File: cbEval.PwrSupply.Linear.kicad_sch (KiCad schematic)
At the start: 38 parts, among them J1 CAL.CT3151V1-0, J10 Socket.Hor.2x5.6-5535512-4, J2 CAL.CT3151V1-2, J3 Keystone.4918, J4 Keystone.4918, J5 Keystone.3571, J6 Keystone.3571, J7 Socket.Hor.2x5.6-5535512-4, J8 Header.Hor.2x5.9-103326-0-05, J9 Header.Hor.2x5.9-103326-0-05, U1 MIC29151-5.0WU, U2 MIC29151-3.3WU, U3 DS1834AS+

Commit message: Bus-Leitungen neu belegt
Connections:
- net PwrBus-Rsrvd0 is gone; now on net I2C-SDA: J7.9, J8.9
- net PwrBus-Rsrvd1 is gone; now on net I2C-SCL: J7.10, J8.10
- net I2C-SCL: no longer J10.10, J9.10
- net I2C-SDA: no longer J10.9, J9.9
- new net One-Wire: J10.10, J9.10
- new net SPI-ADR2: J10.9, J9.9
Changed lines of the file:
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@@
     (stroke (width 0) (type solid) (color 0 0 0 0))
   )
-  (label "PwrBus-Rsrvd0" (at 53.34 182.88 0)
+  (label "I2C-SDA" (at 45.72 182.88 0)
     (effects (font (size 1.27 1.27)) (justify left bottom))
   )
-  (label "PwrBus-Rsrvd1" (at 53.34 185.42 0)
+  (label "I2C-SCL" (at 45.72 185.42 0)
     (effects (font (size 1.27 1.27)) (justify left bottom))
   )
@@
     (effects (font (size 1.27 1.27)) (justify left bottom))
   )
-  (label "I2C-SDA" (at 119.38 182.88 0)
+  (label "SPI-ADR2" (at 119.38 182.88 0)
     (effects (font (size 1.27 1.27)) (justify left bottom))
   )
-  (label "I2C-SCL" (at 119.38 185.42 0)
+  (label "One-Wire" (at 119.38 185.42 0)
     (effects (font (size 1.27 1.27)) (justify left bottom))
   )
@@
     (pin "1")
   )
-  (symbol (lib_name "Supply:GND_6") (lib_id "Supply:GND") (at 35.56 101.6 0) (unit 1)
+  (symbol (lib_id "Supply:GND") (at 35.56 101.6 0) (unit 1)
     (in_bom yes) (on_board yes)
     (property "Reference" "#PWR01" (id 0) (at 35.56 106.68 0)
@@
     (pin "1")
   )
-  (symbol (lib_name "Supply:GND_10") (lib_id "Supply:GND") (at 71.12 101.6 0) (unit 1)
+  (symbol (lib_id "Supply:GND") (at 71.12 101.6 0) (unit 1)
     (in_bom yes) (on_board yes)
     (property "Reference" "#PWR04" (id 0) (at 71.12 106.68 0)
@@
     (pin "1")
   )
-  (symbol (lib_name "Supply:GND_9") (lib_id "Supply:GND") (at 104.14 55.88 0) (unit 1)
+  (symbol (lib_id "Supply:GND") (at 104.14 55.88 0) (unit 1)
     (in_bom yes) (on_board yes)
     (property "Reference" "#PWR07" (id 0) (at 104.14 60.96 0)
@@
     (pin "1")
   )
-  (symbol (lib_name "Supply:GND_4") (lib_id "Supply:GND") (at 127 55.88 0) (unit 1)
+  (symbol (lib_id "Supply:GND") (at 127 55.88 0) (unit 1)
     (in_bom yes) (on_board yes)
     (property "Reference" "#PWR09" (id 0) (at 127 60.96 0)
@@
     (pin "1")
   )
-  (symbol (lib_name "Supply:GND_1") (lib_id "Supply:GND") (at 127 101.6 0) (unit 1)
+  (symbol (lib_id "Supply:GND") (at 127 101.6 0) (unit 1)
     (in_bom yes) (on_board yes)
     (property "Reference" "#PWR011" (id 0) (at 127 106.68 0)
@@
     (pin "1")
   )
-  (symbol (lib_name "Supply:GND_3") (lib_id "Supply:GND") (at 165.1 55.88 0) (unit 1)
+  (symbol (lib_id "Supply:GND") (at 165.1 55.88 0) (unit 1)
     (in_bom yes) (on_board yes)
     (property "Reference" "#PWR013" (id 0) (at 165.1 60.96 0)
@@
     (pin "1")
   )
-  (symbol (lib_name "Supply:GND_2") (lib_id "Supply:GND") (at 165.1 101.6 0) (unit 1)
+  (symbol (lib_id "Supply:GND") (at 165.1 101.6 0) (unit 1)
     (in_bom yes) (on_board yes)
     (property "Reference" "#PWR014" (id 0) (at 165.1 106.68 0)
@@
     (pin "1")
   )
-  (symbol (lib_name "Supply:GND_7") (lib_id "Supply:GND") (at 193.04 55.88 0) (unit 1)
+  (symbol (lib_id "Supply:GND") (at 193.04 55.88 0) (unit 1)
     (in_bom yes) (on_board yes)
     (property "Reference" "#PWR015" (id 0) (at 193.04 60.96 0)
@@
     (pin "1")
   )
-  (symbol (lib_name "Supply:GND_8") (lib_id "Supply:GND") (at 193.04 101.6 0) (unit 1)
+  (symbol (lib_id "Supply:GND") (at 193.04 101.6 0) (unit 1)
     (in_bom yes) (on_board yes)
     (property "Reference" "#PWR016" (id 0) (at 193.04 106.68 0)
@@
       (effects (font (size 0.635 0.635) italic))
     )
-    (property "Usage" "GND Extension" (id 5) (at 25.4 86.36 0))
-    (pin "1")
-  )
-  (symbol (lib_name "J.QuickConnect:Keystone.4918_1") (lib_id "J.QuickConnect:Keystone.4918") (at 27.94 96.52 0) (mirror y) (unit 1)
+    (property "Usage" "GND Extension" (id 6) (at 25.4 86.36 0))
+    (pin "1")
+  )
+  (symbol (lib_id "J.QuickConnect:Keystone.4918") (at 27.94 96.52 0) (mirror y) (unit 1)
     (in_bom yes) (on_board yes)
     (property "Reference" "J4" (id 0) (at 25.4 91.44 0))
@@
       (effects (font (size 0.635 0.635) italic))
     )
-    (property "Usage" "GND Extension" (id 5) (at 25.4 99.06 0))
+    (property "Usage" "GND Extension" (id 6) (at 25.4 99.06 0))
     (pin "1")
   )
@@
       (effects (font (size 0.635 0.635) italic))
     )
-    (property "Usage" "GND Extension" (id 5) (at 45.72 86.36 0))
-    (pin "1")
-  )
-  (symbol (lib_name "J.QuickConnect:Keystone.3571_1") (lib_id "J.QuickConnect:Keystone.3571") (at 43.18 96.52 0) (unit 1)
+    (property "Usage" "GND Extension" (id 6) (at 45.72 86.36 0))
+    (pin "1")
+  )
+  (symbol (lib_id "J.QuickConnect:Keystone.3571") (at 43.18 96.52 0) (unit 1)
     (in_bom yes) (on_board yes)
     (property "Reference" "J6" (id 0) (at 45.72 91.44 0))
@@
       (effects (font (size 0.635 0.635) italic))
     )
-    (property "Usage" "GND Extension" (id 5) (at 45.72 99.06 0))
+    (property "Usage" "GND Extension" (id 6) (at 45.72 99.06 0))
     (pin "1")
   )
@@
       (effects (font (size 0.635 0.635) italic))
     )
-    (property "Usage" "Pwr Supply V+" (id 6) (at 71.12 35.56 0))
-    (pin "1")
-  )
+    (property "Usage" "Pwr Supply V+" (id 7) (at 71.12 35.56 0))
+    (pin "1")
+  )

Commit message: Bauteil (PinHeader) ausgetauscht
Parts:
- J11: renamed from JP3; symbol JP:Bergstik-II_6 -> J.PinHeader:Bergstik-II_6
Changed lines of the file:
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@@
     (pin "6")
   )
-  (symbol (lib_id "JP:Bergstik-II_6") (at 43.18 40.64 0) (unit 1)
-    (in_bom yes) (on_board yes)
-    (property "Reference" "JP3" (id 0) (at 40.64 50.8 0)
+  (symbol (lib_id "J.PinHeader:Bergstik-II_6") (at 43.18 40.64 0) (unit 1)
+    (in_bom yes) (on_board yes)
+    (property "Reference" "J11" (id 0) (at 40.64 50.8 0)
       (effects (font (size 1.27 1.27)) (justify left))
     )
@@
     )
     (path "/fae6516a-9429-461a-8ec1-3b1a99f8be92"
-      (reference "JP3") (unit 1) (value "Bergstik-II_6") (footprint "Connector_PinHeader_2.54mm:PinHeader_1x06_P2.54mm_Vertical")
+      (reference "J11") (unit 1) (value "Bergstik-II_6") (footprint "Connector_PinHeader_2.54mm:PinHeader_1x06_P2.54mm_Vertical")
     )
     (path "/aa3513d0-0eee-457c-a792-7c9954431f2c"

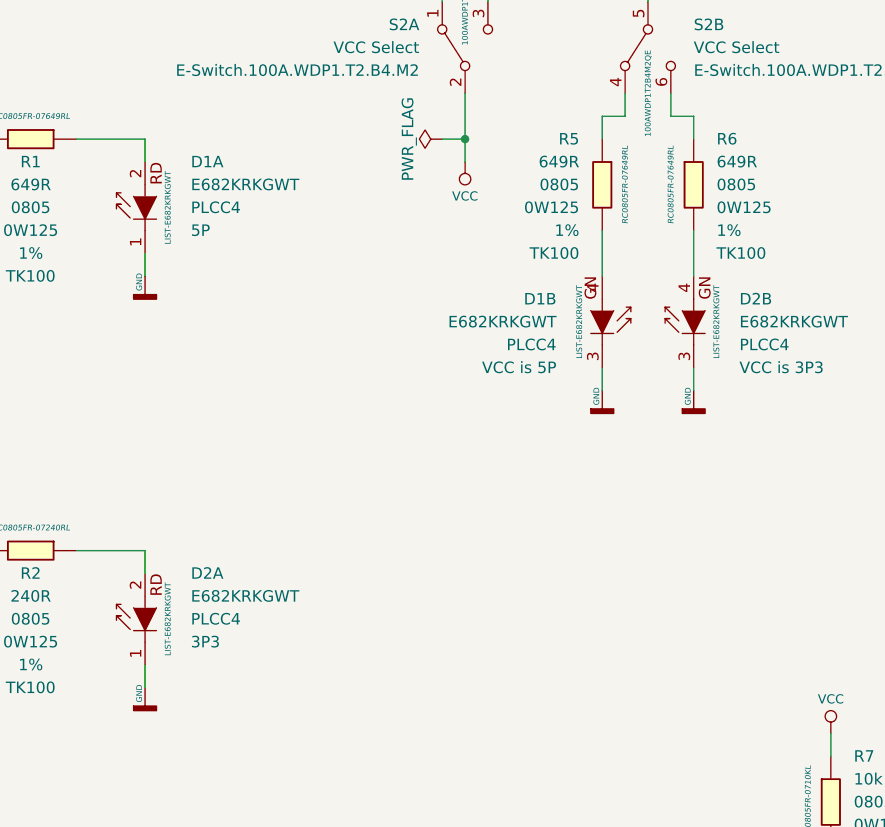
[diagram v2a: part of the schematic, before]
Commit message: kleinere Korrekturen vor Bauteilbestellung
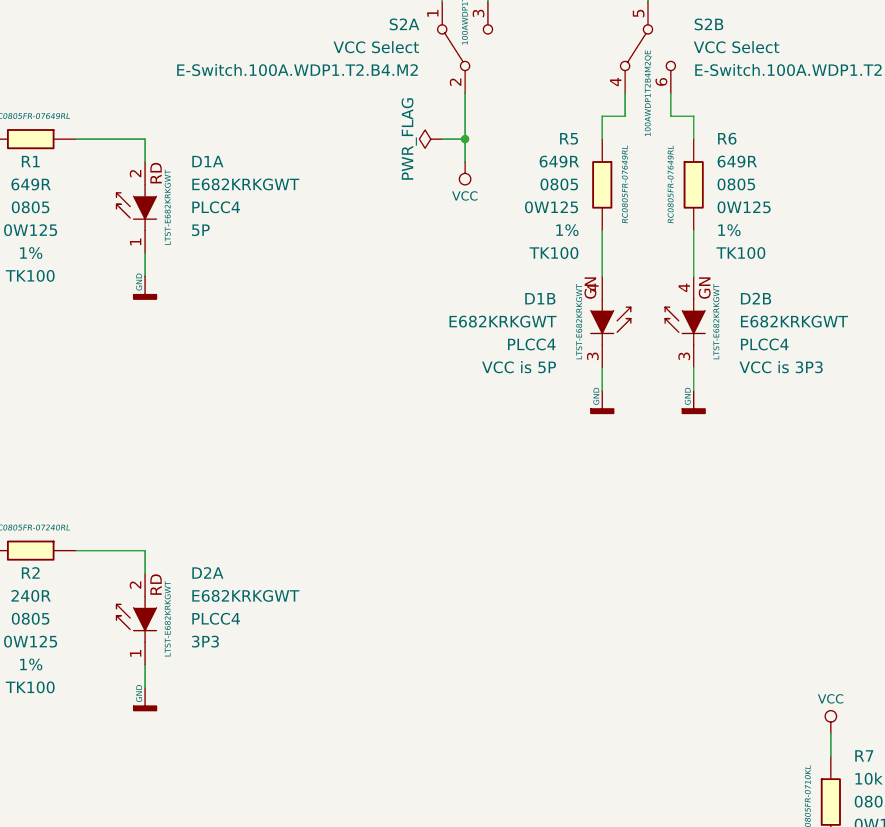
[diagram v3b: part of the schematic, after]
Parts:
- D1, D2: ID LIST-E682KRKGWT -> LTST-E682KRKGWT
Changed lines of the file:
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@@
     (pin "1")
   )
-  (symbol (lib_id "D.LED:E682KRKGWT") (at 193.04 48.26 0) (unit 1)
+  (symbol (lib_name "D.LED:E682KRKGWT_1") (lib_id "D.LED:E682KRKGWT") (at 193.04 48.26 0) (unit 1)
     (in_bom yes) (on_board yes)
     (property "Reference" "D1" (id 0) (at 198.12 43.18 0)
@@
       (effects (font (size 1.27 1.27)) (justify left))
     )
-    (property "ID" "LIST-E682KRKGWT" (id 5) (at 195.58 48.26 90)
+    (property "ID" "LTST-E682KRKGWT" (id 5) (at 195.58 48.26 90)
       (effects (font (size 0.635 0.635)))
     )
@@
       (effects (font (size 1.27 1.27)) (justify left))
     )
-    (property "ID" "LIST-E682KRKGWT" (id 5) (at 195.58 93.98 90)
+    (property "ID" "LTST-E682KRKGWT" (id 5) (at 195.58 93.98 90)
       (effects (font (size 0.635 0.635)))
     )
@@
     (pin "2")
   )
-  (symbol (lib_id "D.LED:E682KRKGWT") (at 243.84 60.96 0) (mirror y) (unit 2)
+  (symbol (lib_name "D.LED:E682KRKGWT_2") (lib_id "D.LED:E682KRKGWT") (at 243.84 60.96 0) (mirror y) (unit 2)
     (in_bom yes) (on_board yes)
     (property "Reference" "D1" (id 0) (at 238.76 58.42 0)
@@
       (effects (font (size 1.27 1.27)) (justify left))
     )
-    (property "ID" "LIST-E682KRKGWT" (id 5) (at 241.3 60.96 90)
+    (property "ID" "LTST-E682KRKGWT" (id 5) (at 241.3 60.96 90)
       (effects (font (size 0.635 0.635)))
     )
@@
     (pin "4")
   )
-  (symbol (lib_id "D.LED:E682KRKGWT") (at 254 60.96 0) (unit 2)
+  (symbol (lib_name "D.LED:E682KRKGWT_3") (lib_id "D.LED:E682KRKGWT") (at 254 60.96 0) (unit 2)
     (in_bom yes) (on_board yes)
     (property "Reference" "D2" (id 0) (at 259.08 58.42 0)
@@
       (effects (font (size 1.27 1.27)) (justify left))
     )
-    (property "ID" "LIST-E682KRKGWT" (id 5) (at 256.54 60.96 90)
+    (property "ID" "LTST-E682KRKGWT" (id 5) (at 256.54 60.96 90)
       (effects (font (size 0.635 0.635)))
     )

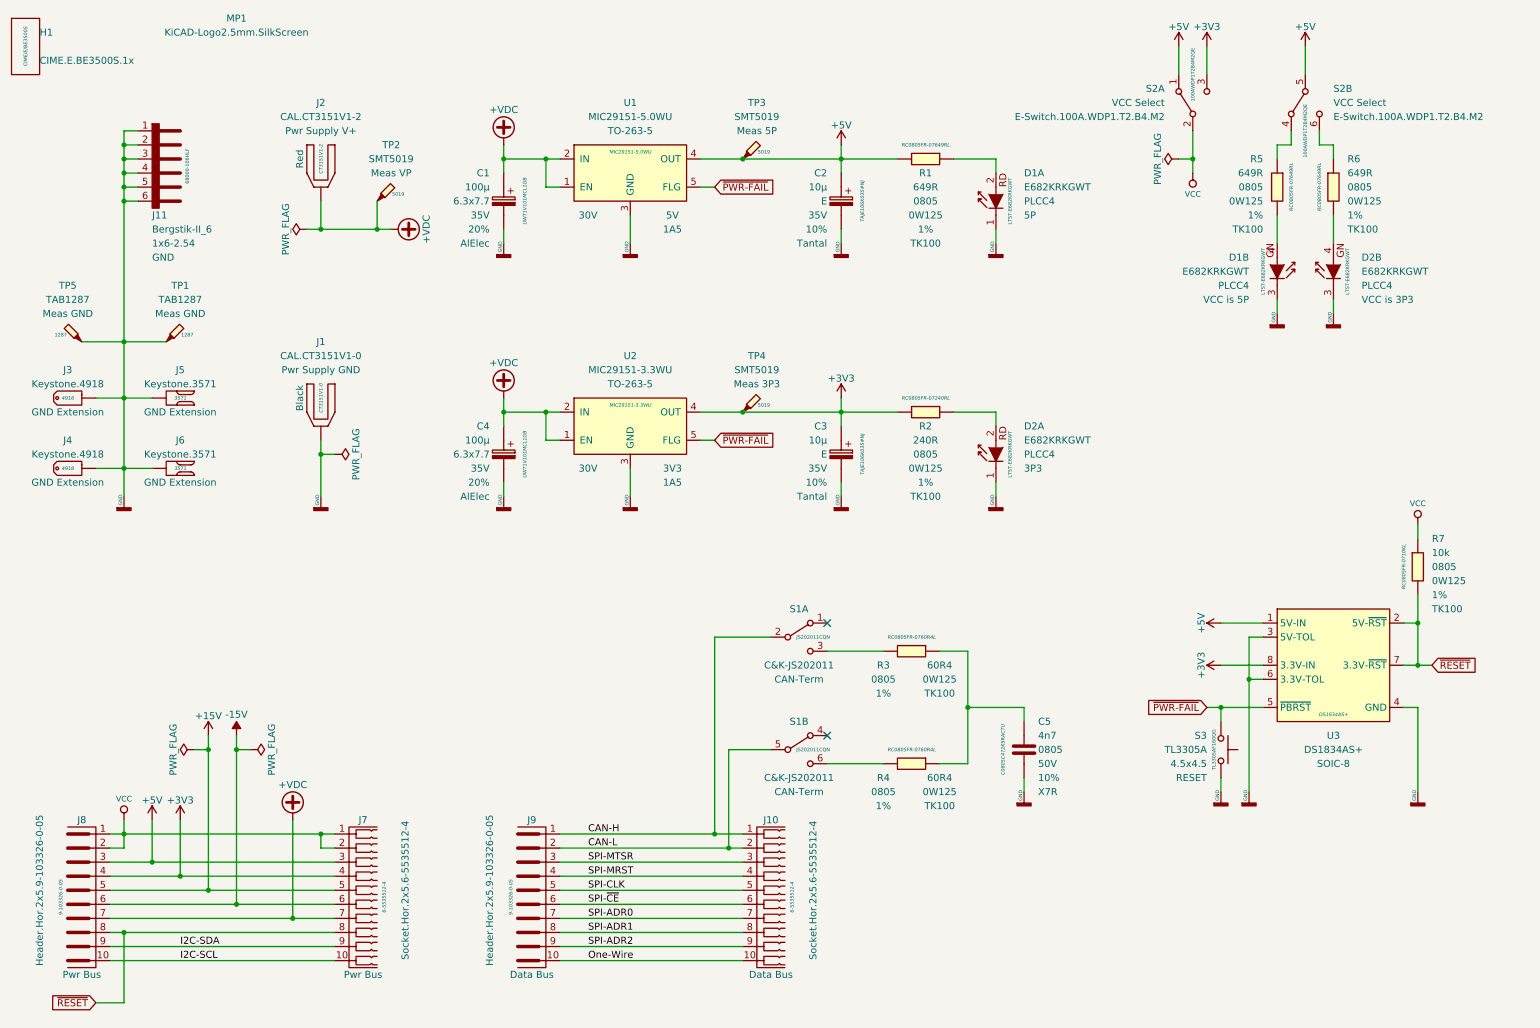
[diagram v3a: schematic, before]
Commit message: Bus-Stecker getauscht
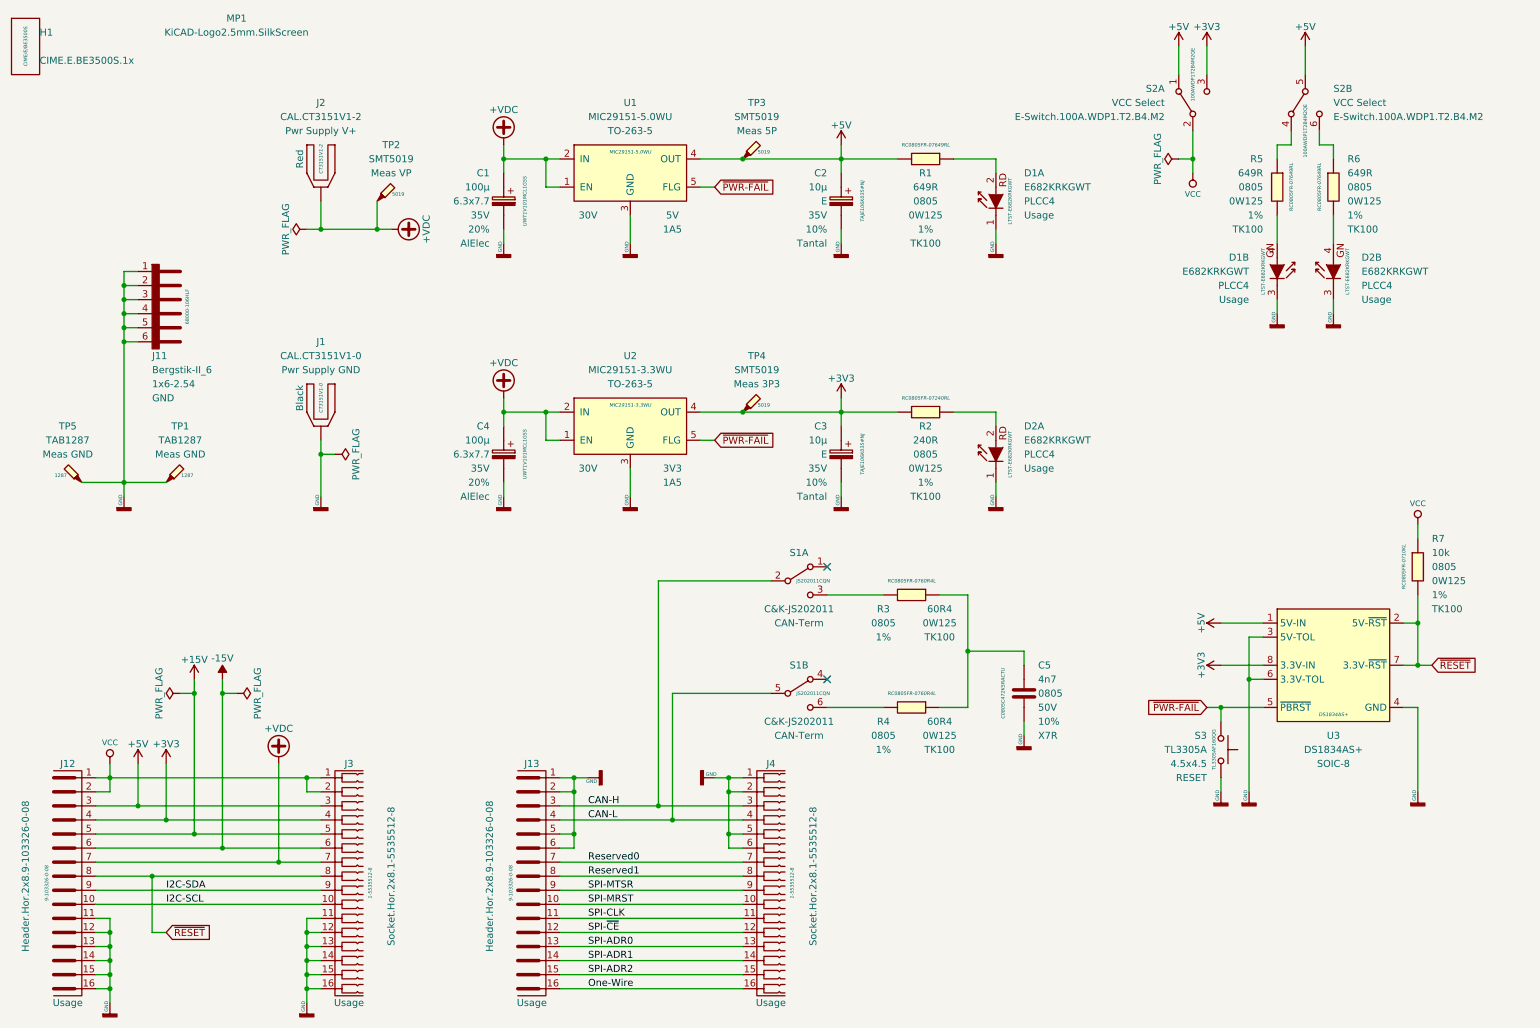
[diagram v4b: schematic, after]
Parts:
- removed J10, J7: Socket.Hor.2x5.6-5535512-4, BTech.Connector.AMPMODU-ModII:Socket.Hor.2x5.6-5535512-4, symbol J.AMPMODU-ModII:Socket.Hor.2x5.6-5535512-4
- removed J3, J4: Keystone.4918, BTech.Connector.QuickConnect:Keystone.4918, symbol J.QuickConnect:Keystone.4918
- removed J5, J6: Keystone.3571, BTech.Connector.QuickConnect:Keystone.3571, symbol J.QuickConnect:Keystone.3571
- removed J8, J9: Header.Hor.2x5.9-103326-0-05, Connector_PinHeader_2.54mm:PinHeader_2x05_P2.54mm_Horizontal, symbol J.AMPMODU-ModII:Header.Hor.2x5.9-103326-0-05
- added J12, J13: Header.Hor.2x8.9-103326-0-08, Connector_PinHeader_2.54mm:PinHeader_2x08_P2.54mm_Horizontal, symbol J.AMPMODU-ModII:Header.Hor.2x8.9-103326-0-08
- added J3, J4: Socket.Hor.2x8.1-5535512-8, BTech.Connector.AMPMODU-ModII:Socket.Hor.2x5.6-5535512-4, symbol J.AMPMODU-ModII:Socket.Hor.2x8.1-5535512-8
- C1, C4: ID UWT1V101MCL1GB -> UWT1V101MCL1G5S
- D1: Usage VCC is 5P -> Usage
- D1: Usage 5P -> Usage
- D2: Usage 3P3 -> Usage
- D2: Usage VCC is 3P3 -> Usage
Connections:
- net +15V: now also J12.5, J3.5
- net +3V3: now also J12.4, J3.4
- net +5V: now also J12.3, J3.3
- net +VDC: now also J12.7, J3.7
- net -15V: now also J12.6, J3.6
- net CAN-H: now also J13.3, J4.3
- net CAN-L: now also J13.4, J4.4
- net GND: now also J12.11, J12.12, J12.13, J12.14, J12.15, J12.16, J13.1, J13.2, J13.5, J13.6, J3.11, J3.12, J3.13, J3.14, J3.15, J3.16, J4.1, J4.2, J4.5, J4.6
- net I2C-SCL: now also J12.10, J3.10
- net I2C-SDA: now also J12.9, J3.9
- net One-Wire: now also J13.16, J4.16
- net SPI-ADR0: now also J13.13, J4.13
- net SPI-ADR1: now also J13.14, J4.14
- net SPI-ADR2: now also J13.15, J4.15
- net SPI-CLK: now also J13.11, J4.11
- net SPI-MRST: now also J13.10, J4.10
- net SPI-MTSR: now also J13.9, J4.9
- net SPI-~CE: now also J13.12, J4.12
- net VCC: now also J12.1, J12.2, J3.1, J3.2
- net ~RESET: now also J12.8, J3.8
- new net Reserved0: J13.7, J4.7
- new net Reserved1: J13.8, J4.8
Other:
- moved on the sheet: C5, J11, R3, R4, S1A, S1B, TP1, TP5
